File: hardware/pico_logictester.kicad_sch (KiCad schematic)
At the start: 29 parts, among them J1 LOGIC_INPUT, J2 GPIO_5_28, J3 AKKU, J4 STEP_UP_IN, J5 5V VERSORGUNG, J6 TFT Display, Q1 AO3401A, Q2 BC547, SW1 SW_Push, U1 74HC245, U2 74HC245

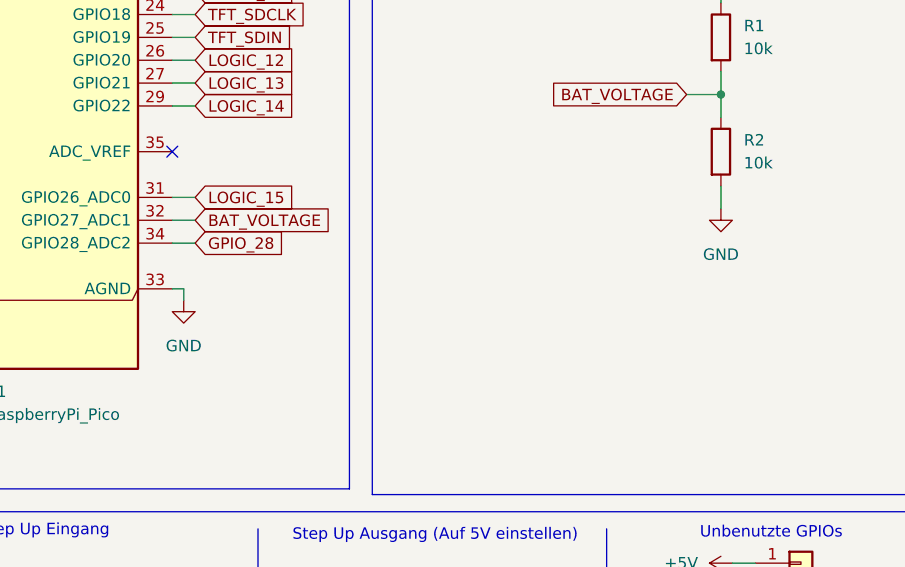
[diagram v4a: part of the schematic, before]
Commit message: hardware: ERC Error behoben
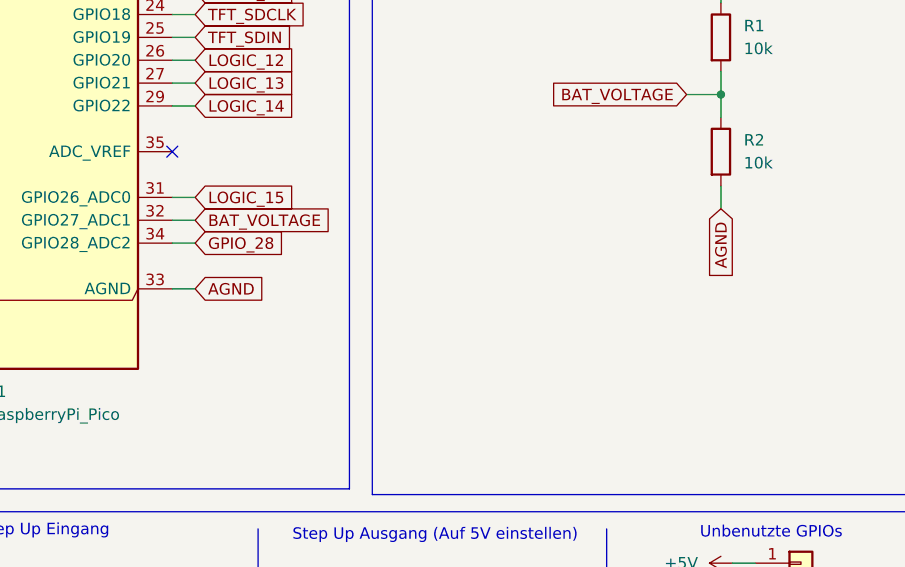
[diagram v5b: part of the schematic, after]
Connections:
- net GND: no longer A1.33 (AGND), R2.2
- new net AGND: A1.33 (AGND), R2.2
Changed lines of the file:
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@@
 	(wire
 		(pts
-			(xy 87.63 85.09) (xy 87.63 86.36)
-		)
-		(stroke
-			(width 0)
-			(type default)
-		)
-	)
-	(wire
-		(pts
 			(xy 196.85 144.78) (xy 195.58 144.78)
 		)
@@
 	(wire
 		(pts
-			(xy 86.36 85.09) (xy 87.63 85.09)
+			(xy 86.36 85.09) (xy 88.9 85.09)
 		)
 		(stroke
@@
 		)
 	)
+	(global_label "AGND"
+		(shape input)
+		(at 147.32 76.2 270)
+		(fields_autoplaced yes)
+		(effects
+			(font
+				(size 1.27 1.27)
+			)
+			(justify right)
+		)
+		(property "Intersheetrefs" "${INTERSHEET_REFS}"
+			(at 147.32 84.1443 90)
+			(effects
+				(font
+					(size 1.27 1.27)
+				)
+				(justify right)
+				(hide yes)
+			)
+		)
+	)
 	(global_label "LOGIC_10"
 		(shape input)
@@
 		)
 	)
+	(global_label "AGND"
+		(shape input)
+		(at 88.9 85.09 0)
+		(fields_autoplaced yes)
+		(effects
+			(font
+				(size 1.27 1.27)
+			)
+			(justify left)
+		)
+		(property "Intersheetrefs" "${INTERSHEET_REFS}"
+			(at 96.8443 85.09 0)
+			(effects
+				(font
+					(size 1.27 1.27)
+				)
+				(justify left)
+				(hide yes)
+			)
+		)
+	)
 	(global_label "LOGIC_7"
 		(shape input)
@@
 	(symbol
 		(lib_id "power:GND")
-		(at 147.32 76.2 0)
-		(unit 1)
-		(exclude_from_sim no)
-		(in_bom yes)
-		(on_board yes)
-		(dnp no)
-		(fields_autoplaced yes)
-		(property "Reference" "#PWR025"
-			(at 147.32 82.55 0)
-			(effects
-				(font
-					(size 1.27 1.27)
-				)
-				(hide yes)
-			)
-		)
-		(property "Value" "GND"
-			(at 147.32 81.28 0)
-			(effects
-				(font
-					(size 1.27 1.27)
-				)
-			)
-		)
-		(property "Footprint" ""
-			(at 147.32 76.2 0)
-			(effects
-				(font
-					(size 1.27 1.27)
-				)
-				(hide yes)
-			)
-		)
-		(property "Datasheet" ""
-			(at 147.32 76.2 0)
-			(effects
-				(font
-					(size 1.27 1.27)
-				)
-				(hide yes)
-			)
-		)
-		(property "Description" "Power symbol creates a global label with name \"GND\" , ground"
-			(at 147.32 76.2 0)
-			(effects
-				(font
-					(size 1.27 1.27)
-				)
-				(hide yes)
-			)
-		)
-		(pin "1"
-		)
-		(instances
-			(project ""
-				(path "/ab4c5817-8853-4523-896c-e7a16e8d82cb"
-					(reference "#PWR025")
-					(unit 1)
-				)
-			)
-		)
-	)
-	(symbol
-		(lib_id "power:GND")
 		(at 195.58 73.66 0)
 		(unit 1)
@@
 					(unit 1)
 				)
-			)
-		)
-	)
-	(symbol
-		(lib_id "power:GND")
-		(at 87.63 86.36 0)
-		(unit 1)
-		(exclude_from_sim no)
-		(in_bom yes)
-		(on_board yes)
-		(dnp no)
-		(fields_autoplaced yes)
-		(property "Reference" "#PWR02"
-			(at 87.63 92.71 0)
-			(effects
-				(font
-					(size 1.27 1.27)
-				)
-				(hide yes)
-			)
-		)
-		(property "Value" "GND"
-			(at 87.63 91.44 0)
-			(effects
-				(font
-					(size 1.27 1.27)
-				)
-			)
-		)
-		(property "Footprint" ""
-			(at 87.63 86.36 0)
-			(effects
-				(font
-					(size 1.27 1.27)
-				)
-				(hide yes)
-			)
-		)
-		(property "Datasheet" ""
-			(at 87.63 86.36 0)
-			(effects
-				(font
-					(size 1.27 1.27)
-				)
-				(hide yes)
-			)
-		)
-		(property "Description" "Power symbol creates a global label with name \"GND\" , ground"
-			(at 87.63 86.36 0)
-			(effects
-				(font
-					(size 1.27 1.27)
-				)
-				(hide yes)
-			)
-		)
-		(pin "1"
-		)
-		(instances
-			(project ""
-				(path "/ab4c5817-8853-4523-896c-e7a16e8d82cb"
-					(reference "#PWR02")
-					(unit 1)
-				)

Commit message: hardware: new pcb layout
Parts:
- removed J1: LOGIC_INPUT, Connector_IDC:IDC-Header_2x08_P2.54mm_Horizontal, symbol Connector_Generic:Conn_02x08_Odd_Even
- added J1: LOGIC_INPUT, Connector_IDC:IDC-Header_2x09_P2.54mm_Horizontal, symbol Connector_Generic:Conn_02x09_Odd_Even
- SW1: footprint Button_Switch_THT:SW_PUSH_6mm_H5mm -> Button_Switch_THT:SW_Tactile_SPST_Angled_PTS645Vx83-2LFS
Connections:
- net GND: now also J1.17 (Pin_17), J1.18 (Pin_18)
- net LOGIC10: now also J1.6 (Pin_6)
- net LOGIC11: now also J1.8 (Pin_8)
- net LOGIC12: now also J1.10 (Pin_10)
- net LOGIC13: now also J1.12 (Pin_12)
- net LOGIC14: now also J1.14 (Pin_14)
- net LOGIC15: now also J1.16 (Pin_16)
- net LOGIC8: now also J1.2 (Pin_2)
- net LOGIC9: now also J1.4 (Pin_4)
- net at RN1.1 (R1.1): now also J1.15 (Pin_15)
- net at RN1.2 (R2.1): now also J1.13 (Pin_13)
- net at RN1.3 (R3.1): now also J1.11 (Pin_11)
- net at RN1.4 (R4.1): now also J1.9 (Pin_9)
- net at RN1.5 (R5.1): now also J1.7 (Pin_7)
- net at RN1.6 (R6.1): now also J1.5 (Pin_5)
- net at RN1.7 (R7.1): now also J1.3 (Pin_3)
- net at RN1.8 (R8.1): now also J1.1 (Pin_1)
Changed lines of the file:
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@@
 	(wire
 		(pts
+			(xy 270.51 67.31) (xy 271.78 67.31)
+		)
+		(stroke
+			(width 0)
+			(type default)
+		)
+	)
+	(wire
+		(pts
 			(xy 86.36 54.61) (xy 88.9 54.61)
 		)
@@
 	(wire
 		(pts
+			(xy 271.78 67.31) (xy 271.78 68.58)
+		)
+		(stroke
+			(width 0)
+			(type default)
+		)
+	)
+	(wire
+		(pts
 			(xy 196.85 144.78) (xy 195.58 144.78)
 		)
@@
 	(wire
 		(pts
+			(xy 257.81 67.31) (xy 256.54 67.31)
+		)
+		(stroke
+			(width 0)
+			(type default)
+		)
+	)
+	(wire
+		(pts
 			(xy 127 138.43) (xy 129.54 138.43)
 		)
@@
 	(wire
 		(pts
+			(xy 256.54 67.31) (xy 256.54 68.58)
+		)
+		(stroke
+			(width 0)
+			(type default)
+		)
+	)
+	(wire
+		(pts
 			(xy 223.52 46.99) (xy 243.84 46.99)
 		)
@@
 	)
 	(symbol
+		(lib_id "power:GND")
+		(at 256.54 68.58 0)
+		(unit 1)
+		(exclude_from_sim no)
+		(in_bom yes)
+		(on_board yes)
+		(dnp no)
+		(fields_autoplaced yes)
+		(property "Reference" "#PWR02"
+			(at 256.54 74.93 0)
+			(effects
+				(font
+					(size 1.27 1.27)
+				)
+				(hide yes)
+			)
+		)
+		(property "Value" "GND"
+			(at 256.54 73.66 0)
+			(effects
+				(font
+					(size 1.27 1.27)
+				)
+			)
+		)
+		(property "Footprint" ""
+			(at 256.54 68.58 0)
+			(effects
+				(font
+					(size 1.27 1.27)
+				)
+				(hide yes)
+			)
+		)
+		(property "Datasheet" ""
+			(at 256.54 68.58 0)
+			(effects
+				(font
+					(size 1.27 1.27)
+				)
+				(hide yes)
+			)
+		)
+		(property "Description" "Power symbol creates a global label with name \"GND\" , ground"
+			(at 256.54 68.58 0)
+			(effects
+				(font
+					(size 1.27 1.27)
+				)
+				(hide yes)
+			)
+		)
+		(pin "1"
+		)
+		(instances
+			(project ""
+				(path "/ab4c5817-8853-4523-896c-e7a16e8d82cb"
+					(reference "#PWR02")
+					(unit 1)
+				)
+			)
+		)
+	)
+	(symbol
 		(lib_id "power:+3.3V")
 		(at 68.58 22.86 0)
@@
 			)
 		)
-		(property "Footprint" "Button_Switch_THT:SW_PUSH_6mm_H5mm"
+		(property "Footprint" "Button_Switch_THT:SW_Tactile_SPST_Angled_PTS645Vx83-2LFS"
 			(at 121.92 179.07 0)
 			(effects
@@
 			)
 		)
-		(property "Datasheet" "~"
+		(property "Datasheet" ""
 			(at 121.92 179.07 0)
 			(effects
@@
 			)
 		)
-		(property "Description" "Push button switch, generic, two pins"
+		(property "Description" ""
 			(at 127 179.07 0)
 			(effects
@@
 	)
 	(symbol
+		(lib_id "Connector_Generic:Conn_02x09_Odd_Even")
+		(at 262.89 57.15 0)
+		(unit 1)
+		(exclude_from_sim no)
+		(in_bom yes)
+		(on_board yes)
+		(dnp no)
+		(fields_autoplaced yes)
+		(property "Reference" "J1"
+			(at 264.16 40.64 0)
+			(effects
+				(font
+					(size 1.27 1.27)
+				)
+			)
+		)
+		(property "Value" "LOGIC_INPUT"
+			(at 264.16 43.18 0)
+			(effects
+				(font
+					(size 1.27 1.27)
+				)
+			)
+		)
+		(property "Footprint" "Connector_IDC:IDC-Header_2x09_P2.54mm_Horizontal"
+			(at 262.89 57.15 0)
+			(effects
+				(font
+					(size 1.27 1.27)
+				)
+				(hide yes)
+			)
+		)
+		(property "Datasheet" "~"
+			(at 262.89 57.15 0)
+			(effects
+				(font
+					(size 1.27 1.27)
+				)
+				(hide yes)
+			)
+		)
+		(property "Description" "Generic connector, double row, 02x09, odd/even pin numbering scheme (row 1 odd numbers, row 2 even numbers), script generated (kicad-library-utils/schlib/autogen/connector/)"
+			(at 262.89 57.15 0)
+			(effects
+				(font
+					(size 1.27 1.27)
+				)
+				(hide yes)
+			)
+		)
+		(pin "12"
+		)
+		(pin "8"
+		)
+		(pin "6"
+		)
+		(pin "10"
+		)
+		(pin "17"
+		)
+		(pin "1"
+		)
+		(pin "18"
+		)
+		(pin "4"
+		)
+		(pin "13"
+		)
+		(pin "15"
+		)
+		(pin "14"
+		)
+		(pin "3"
+		)
+		(pin "7"
+		)
+		(pin "16"
+		)
+		(pin "11"
+		)
+		(pin "9"
+		)
+		(pin "2"
+		)
+		(pin "5"
+		)
+		(instances
+			(project ""
+				(path "/ab4c5817-8853-4523-896c-e7a16e8d82cb"
+					(reference "J1")
+					(unit 1)
+				)
+			)
+		)
+	)
+	(symbol
 		(lib_id "power:GND")
 		(at 31.75 124.46 0)
@@
 	)
 	(symbol
-		(lib_id "Connector_Generic:Conn_02x08_Odd_Even")
-		(at 262.89 54.61 0)
-		(unit 1)
-		(exclude_from_sim no)
-		(in_bom yes)
-		(on_board yes)
-		(dnp no)
-		(fields_autoplaced yes)
-		(property "Reference" "J1"
-			(at 264.16 40.64 0)
-			(effects
-				(font
-					(size 1.27 1.27)
-				)
-			)
-		)
-		(property "Value" "LOGIC_INPUT"
-			(at 264.16 43.18 0)
-			(effects
-				(font
-					(size 1.27 1.27)
-				)
-			)
-		)
-		(property "Footprint" "Connector_IDC:IDC-Header_2x08_P2.54mm_Horizontal"
-			(at 262.89 54.61 0)
-			(effects
-				(font
-					(size 1.27 1.27)
-				)
-				(hide yes)
-			)
-		)
-		(property "Datasheet" "~"
-			(at 262.89 54.61 0)
-			(effects
-				(font
-					(size 1.27 1.27)
-				)
-				(hide yes)
-			)
-		)
-		(property "Description" "Generic connector, double row, 02x08, odd/even pin numbering scheme (row 1 odd numbers, row 2 even numbers), script generated (kicad-library-utils/schlib/autogen/connector/)"
-			(at 262.89 54.61 0)
-			(effects
-				(font
-					(size 1.27 1.27)
-				)
-				(hide yes)
-			)
-		)
-		(pin "4"
-		)
-		(pin "12"
-		)
-		(pin "6"
-		)
-		(pin "2"
-		)
-		(pin "11"
-		)
-		(pin "13"
-		)
-		(pin "7"
-		)
-		(pin "1"
-		)
-		(pin "9"
-		)
-		(pin "14"
-		)
-		(pin "8"
-		)
-		(pin "16"
-		)
-		(pin "10"
-		)
-		(pin "15"
-		)
-		(pin "5"
-		)
-		(pin "3"
-		)
-		(instances
-			(project ""
-				(path "/ab4c5817-8853-4523-896c-e7a16e8d82cb"
-					(reference "J1")
-					(unit 1)
-				)
-			)
-		)
-	)
-	(symbol
 		(lib_id "Transistor_BJT:BC547")
 		(at 104.14 170.18 0)
@@
 					(unit 1)
 				)
+			)
+		)
+	)
+	(symbol
+		(lib_id "power:GND")
+		(at 271.78 68.58 0)
+		(unit 1)
+		(exclude_from_sim no)
+		(in_bom yes)
+		(on_board yes)
+		(dnp no)
+		(fields_autoplaced yes)
+		(property "Reference" "#PWR025"
+			(at 271.78 74.93 0)
+			(effects
+				(font
+					(size 1.27 1.27)
+				)
+				(hide yes)
+			)
+		)
+		(property "Value" "GND"
+			(at 271.78 73.66 0)
+			(effects
+				(font
+					(size 1.27 1.27)
+				)
+			)
+		)
+		(property "Footprint" ""
+			(at 271.78 68.58 0)
+			(effects
+				(font
+					(size 1.27 1.27)
+				)
+				(hide yes)
+			)
+		)
+		(property "Datasheet" ""
+			(at 271.78 68.58 0)
+			(effects
+				(font
+					(size 1.27 1.27)
+				)
+				(hide yes)
+			)
+		)
+		(property "Description" "Power symbol creates a global label with name \"GND\" , ground"
+			(at 271.78 68.58 0)
+			(effects
+				(font
+					(size 1.27 1.27)
+				)
+				(hide yes)
+			)
+		)
+		(pin "1"
+		)
+		(instances
+			(project "pico_logictester"
+				(path "/ab4c5817-8853-4523-896c-e7a16e8d82cb"
+					(reference "#PWR025")
+					(unit 1)
+				)

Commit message: remove files
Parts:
- removed J1: LOGIC_INPUT, Connector_IDC:IDC-Header_2x09_P2.54mm_Horizontal, symbol Connector_Generic:Conn_02x09_Odd_Even
- added J1: LOGIC_INPUT, Connector_IDC:IDC-Header_2x08_P2.54mm_Horizontal, symbol Connector_Generic:Conn_02x08_Odd_Even
- SW1: footprint Button_Switch_THT:SW_Tactile_SPST_Angled_PTS645Vx83-2LFS -> Button_Switch_THT:SW_PUSH_6mm_H9.5mm
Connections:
- net AGND is gone; now on net GND: A1.33 (AGND), R2.2
- net LOGIC10: now also J1.6 (Pin_6)
- net LOGIC11: now also J1.8 (Pin_8)
- net LOGIC12: now also J1.10 (Pin_10)
- net LOGIC13: now also J1.12 (Pin_12)
- net LOGIC14: now also J1.14 (Pin_14)
- net LOGIC15: now also J1.16 (Pin_16)
- net LOGIC8: now also J1.2 (Pin_2)
- net LOGIC9: now also J1.4 (Pin_4)
- net at RN1.1 (R1.1): now also J1.15 (Pin_15)
- net at RN1.2 (R2.1): now also J1.13 (Pin_13)
- net at RN1.3 (R3.1): now also J1.11 (Pin_11)
- net at RN1.4 (R4.1): now also J1.9 (Pin_9)
- net at RN1.5 (R5.1): now also J1.7 (Pin_7)
- net at RN1.6 (R6.1): now also J1.5 (Pin_5)
- net at RN1.7 (R7.1): now also J1.3 (Pin_3)
- net at RN1.8 (R8.1): now also J1.1 (Pin_1)
